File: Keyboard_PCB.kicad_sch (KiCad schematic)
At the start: 31 parts, among them J1 USB_C_Receptacle_USB2.0_16P, J2 SWD_Conn, SW1 SW_Push, U1 USBLC6-2SC6, U2 MIC5365-3.3YC5, U3 STM32F401RCT6, Y1 25MHz, Y2 32kHz768

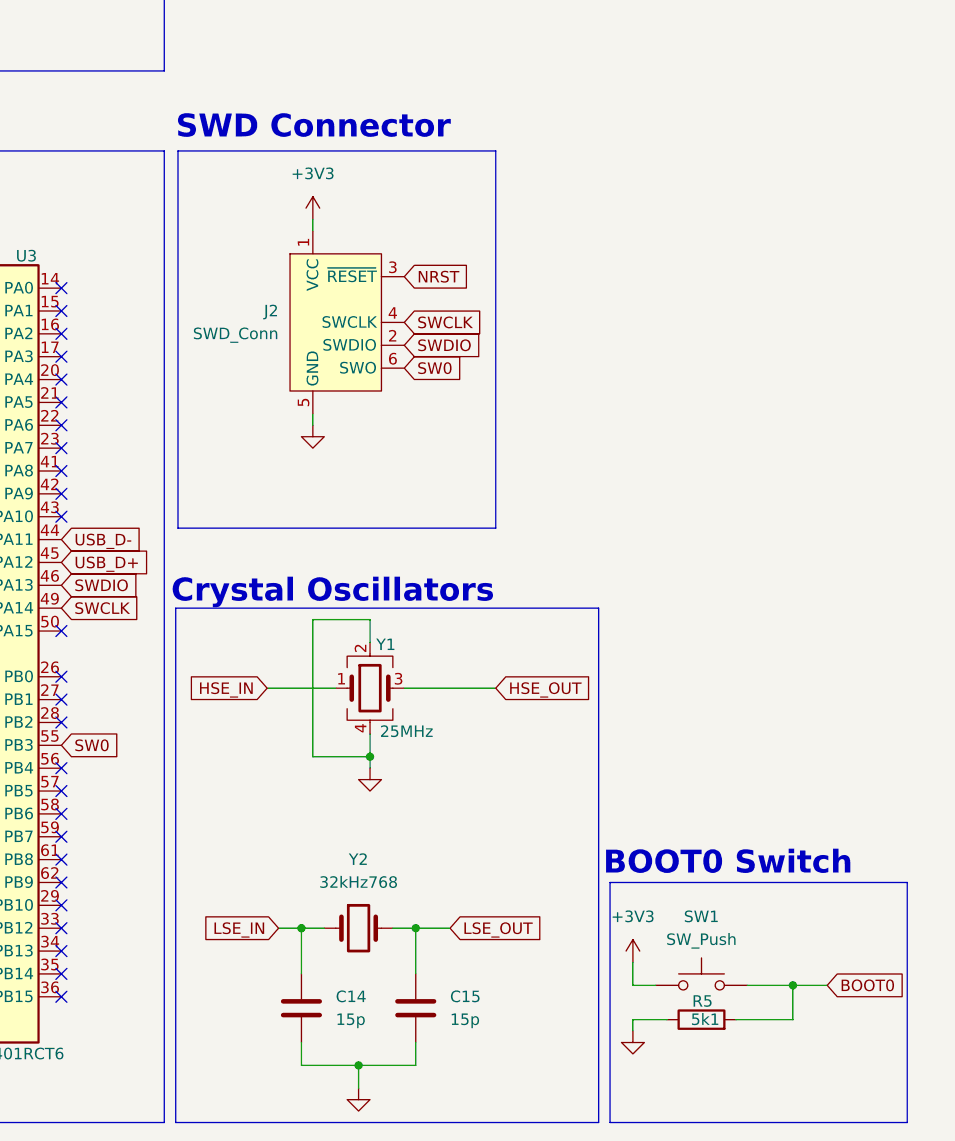
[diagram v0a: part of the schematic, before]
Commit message: Missing Matrix Connection to MCU
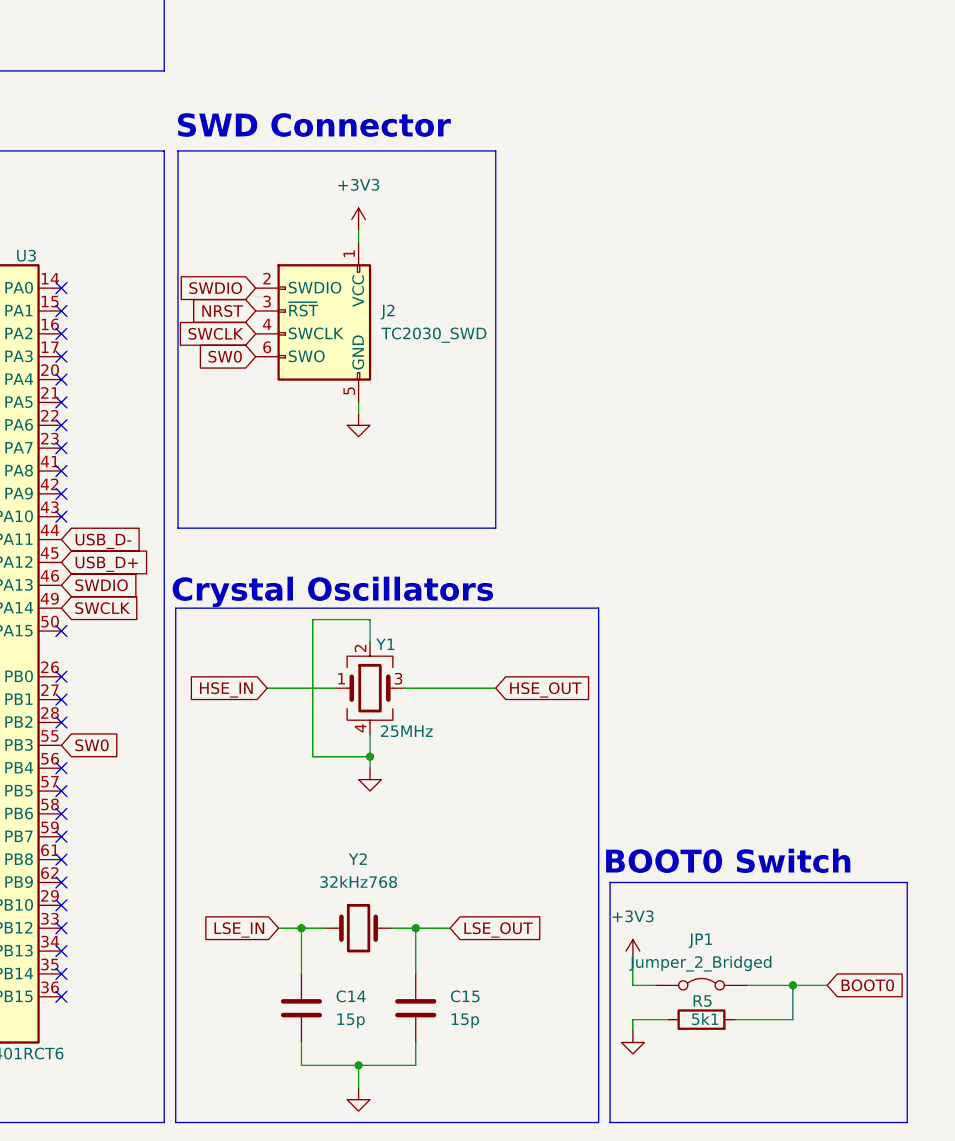
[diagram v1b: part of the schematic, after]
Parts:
- removed J2: SWD_Conn, Connector:Tag-Connect_TC2030-IDC-FP_2x03_P1.27mm_Vertical, symbol Connector:Conn_ARM_SWD_TagConnect_TC2030
- removed SW1: SW_Push, random-keyboard-parts.pretty-master:SKQG-1155865, symbol Switch:SW_Push
- added J2: TC2030_SWD, Connector_IDC:IDC-Header_2x03_P2.54mm_Horizontal, symbol marbastlib-various:TC2030_SWD
- added JP1: Jumper_2_Bridged, TestPoint:TestPoint_2Pads_Pitch2.54mm_Drill0.8mm, symbol Jumper:Jumper_2_Bridged
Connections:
- net +3V3: now also J2.1 (VCC), JP1.1 (A)
- net BOOT0: now also JP1.2 (B)
- net GND: now also J2.5 (GND)
- net NRST: now also J2.3 (~{RST})
- net SW0: now also J2.6 (SWO)
- net SWCLK: now also J2.4 (SWCLK)
- net SWDIO: now also J2.2 (SWDIO)

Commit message: PCB finished
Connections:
- net COL00: now reaches U3.20 (PA4)
- net COL01: now reaches U3.21 (PA5)
- net COL02: now reaches U3.22 (PA6)
- net COL03: now reaches U3.23 (PA7)
- net COL04: now reaches U3.24 (PC4)
- net COL05: now reaches U3.25 (PC5)
- net COL06: now reaches U3.26 (PB0)
- net COL07: now reaches U3.27 (PB1)
- net COL08: now reaches U3.28 (PB2)
- net COL09: now reaches U3.29 (PB10)
- net ROW0: now reaches U3.34 (PB13)
- net ROW1: now reaches U3.35 (PB14)
- net ROW2: now reaches U3.36 (PB15)
- net ROW3: now reaches U3.37 (PC6)
- net ROW4: now reaches U3.38 (PC7)
- net COL10: now reaches U3.39 (PC8)
- net COL11: now reaches U3.40 (PC9)
- net COL12: now reaches U3.41 (PA8)
- net COL13: now reaches U3.42 (PA9)
- net COL14: now reaches U3.43 (PA10)
- no-connect marks 43 -> 23

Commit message: save
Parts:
- added H1, H2, H3, H4, H5, H6: MountingHole, MountingHole:MountingHole_2.2mm_M2, symbol Mechanical:MountingHole
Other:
- note added: "Mounting Holes"
